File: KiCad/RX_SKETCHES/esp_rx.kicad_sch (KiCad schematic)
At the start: 5 parts, among them U2 ESP32-WROOM-32U

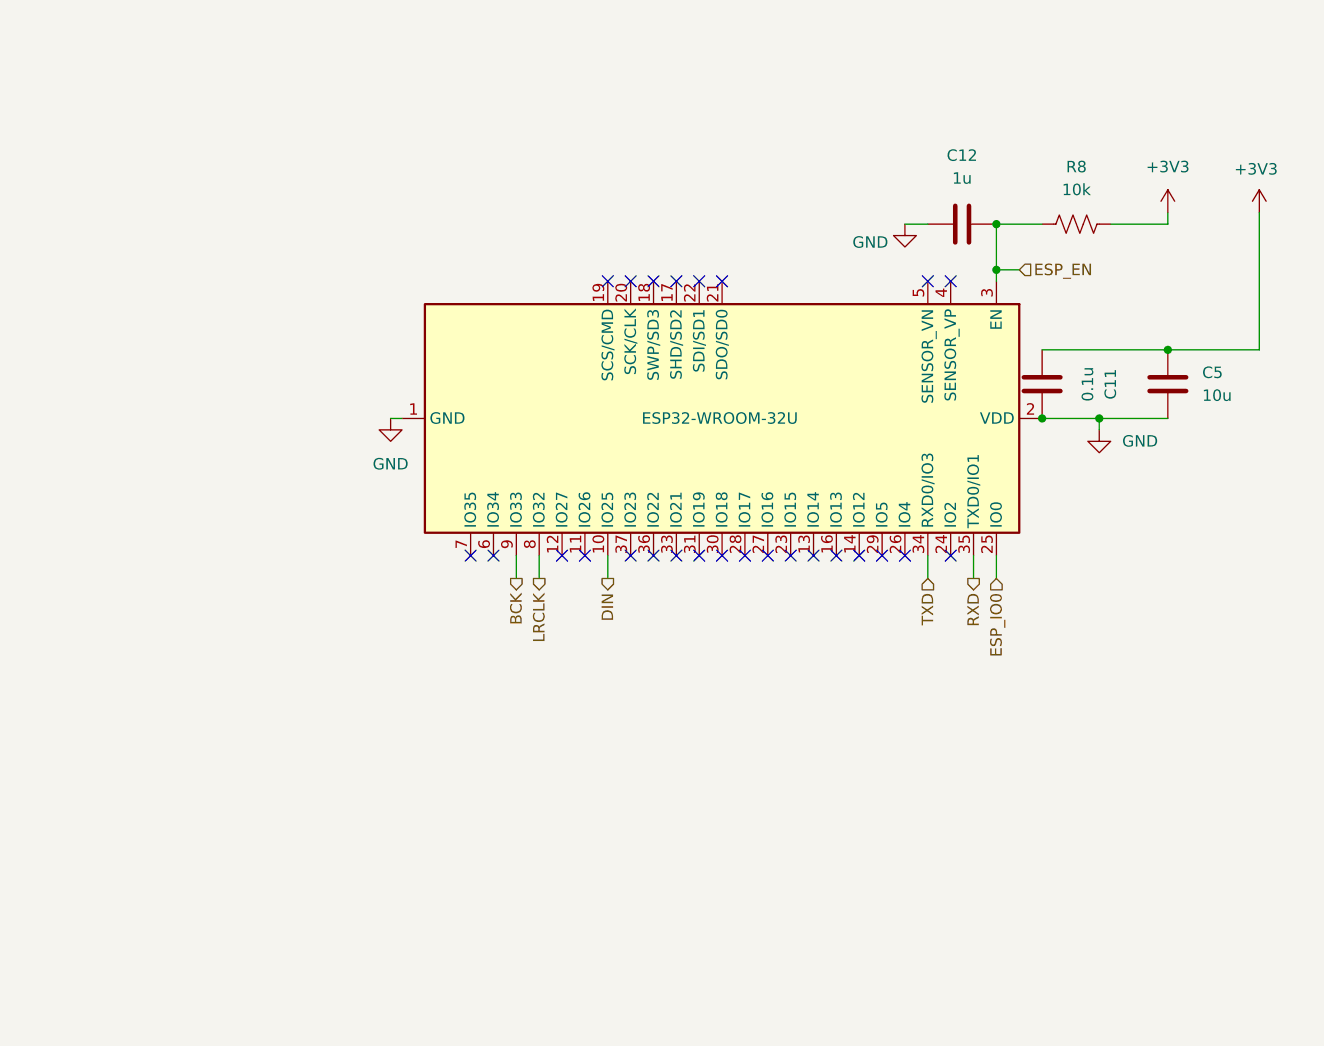
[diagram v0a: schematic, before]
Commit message: RX v1: complete PCB layout, retune analog chain, fix ESD clamp placement
Brings the RX schematic and board up to a fabricable state. DRC is clean:
zero unconnected items, zero schematic-parity issues. The 16 remaining
violations are footprint-inherent and documented rather than worked around
(ESP32-WROOM thermal via array drilled 0.2 mm against a 0.3 mm rule, and
USB-C NPTH-to-pad spacing from the vendor land pattern).

Analog:
- Gain network populated at RF 4.7k / RIN 47k (-20 dB) rather than DNP 10k.
  Tames the PCM5102's 2.1 Vrms into sensitive IEMs, gives the 10k pot a
  4.7x loading ratio instead of 1:1, and lifts the coupling corner clear of
  the audible band.
- Coupling caps C1-C4 raised 0.47uF -> 1uF. Corner 7.2 Hz -> 3.4 Hz, and it
  halves the signal developed across the ceramic at 20 Hz, which is where
  Class-II dielectric distortion actually shows up.
- PCM5102 mode pins no longer float: 100k pulldowns on FLT and XSMT, with
  DEMP and FMT strapped to GND.

Power and protection:
- D1's third TVS channel moved off the switched +5V rail onto VBUS_RAW. An
  ESD clamp has to sit on the connector pin exposed to a finger; behind the
  power switch it disconnected exactly when the board is most likely to be
  handled. The off state is unaffected -- a TVS is open below its standoff
  voltage and SW4 still breaks the rail.
- All three slide switches now follow one rule: the open throw is the safe
  default (powered off / normal-latency filter / muted).

Housekeeping:
- C28 and mounting holes REF1-REF4 added to the schematic, clearing parity
  errors against parts that previously existed only on the PCB.
- Gain, loudness, and filter math written up in README.org with sources so
  the numbers can be re-derived; rationale logged in hardware_revisions.org.
- .gitignore now covers the editor .history/ directory and ESP-IDF build
  output, which were showing up as untracked noise.

Firmware and build artifacts are deliberately excluded from this commit.

Co-authored-b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
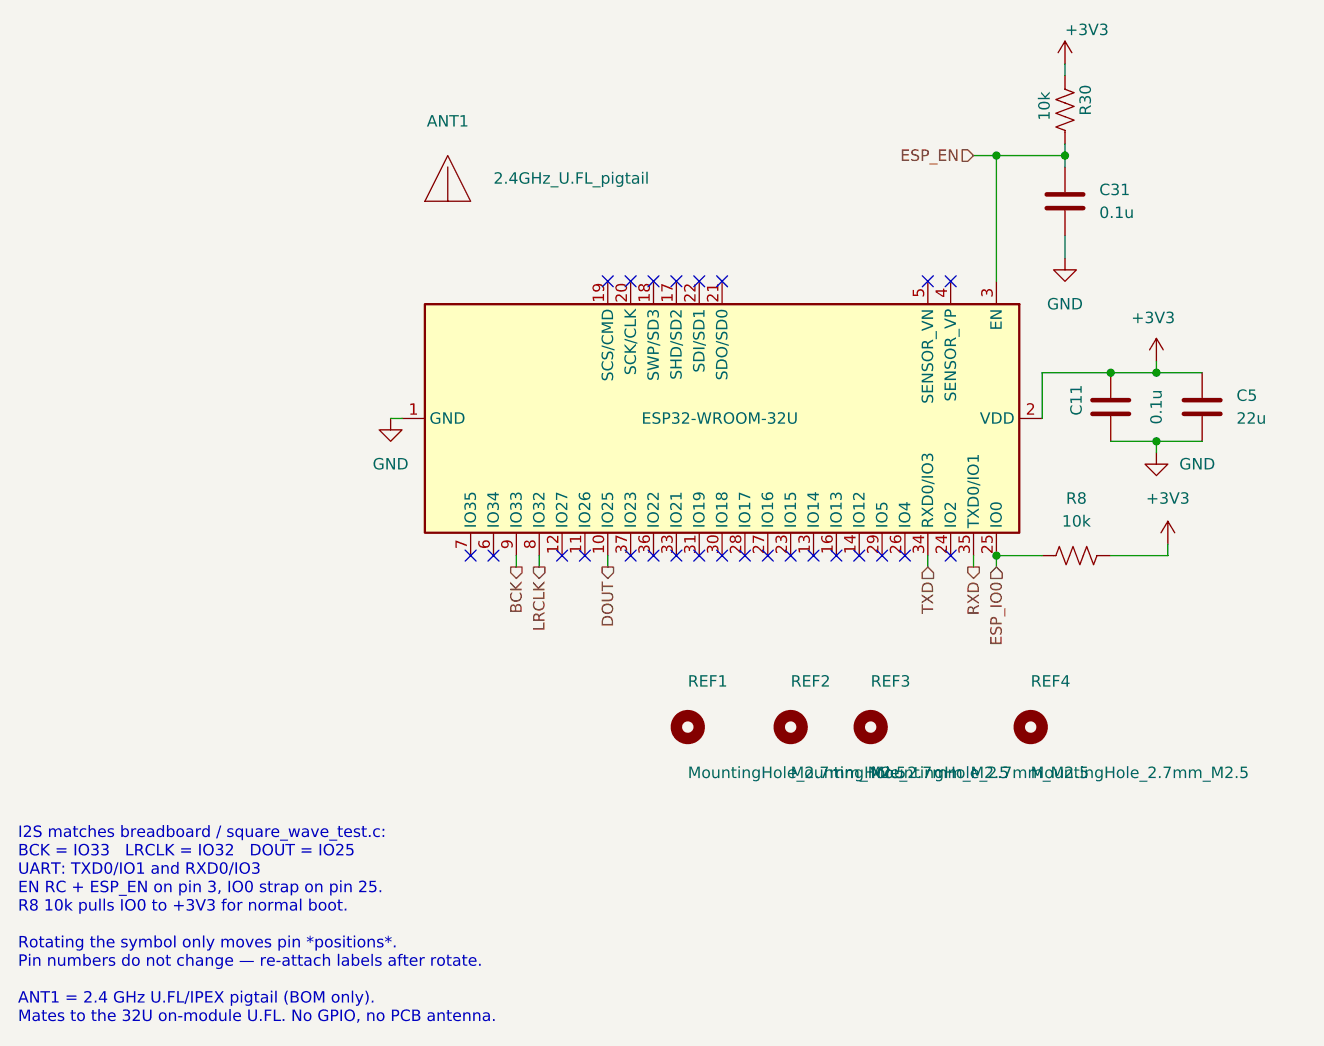
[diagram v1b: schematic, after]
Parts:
- removed C12: 1u, Capacitor_SMD:C_0201_0603Metric, symbol Device:C
- added ANT1: 2.4GHz_U.FL_pigtail, symbol Device:Antenna
- added C31: 0.1u, Capacitor_SMD:C_0805_2012Metric_Pad1.18x1.45mm_HandSolder, symbol Device:C
- added R30: 10k, Resistor_SMD:R_0805_2012Metric_Pad1.20x1.40mm_HandSolder, symbol Device:R_US
- added REF1, REF2, REF3, REF4: MountingHole_2.7mm_M2.5, MountingHole:MountingHole_2.7mm_M2.5, symbol Mechanical:MountingHole
- C11: footprint Capacitor_SMD:C_0201_0603Metric -> Capacitor_SMD:C_0805_2012Metric_Pad1.18x1.45mm_HandSolder
- C5: value 10u -> 22u; footprint Capacitor_SMD:C_0201_0603Metric -> Capacitor_SMD:C_0805_2012Metric_Pad1.18x1.45mm_HandSolder
- R8: footprint Resistor_SMD:R_0201_0603Metric -> Resistor_SMD:R_0805_2012Metric_Pad1.20x1.40mm_HandSolder
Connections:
- net +3V3: now also U2.2 (VDD), R30.2
- net ESP_EN: now also C31.1, R30.1; no longer R8.2
- net ESP_IO0: now also R8.2
- net GND: now also C31.2; no longer U2.2 (VDD)
- net DIN renamed DOUT
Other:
- note added: "I2S matches breadboard / square_wave_test.c: BCK = IO33 LRCLK = IO32 DOUT = IO25 UART: TXD0/IO1 and RXD0/IO3 EN RC + ESP_EN on pin 3, IO0 strap on pin 25. R8 10k pulls IO0 to +3V3 for normal boot. Rotating the symbol only moves pin *positions*. Pin numbers do not change — re-attach labels after rotate. ANT1 = 2.4 GHz U.FL/IPEX pigtail (BOM only). Mates to the 32U on-module U.FL. No GPIO, no PCB a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"
- moved on the sheet: C11, C5, R8
